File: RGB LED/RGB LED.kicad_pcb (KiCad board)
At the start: 2 copper layers, 93.1 x 66.5 mm, 86 parts, among them J1 USB_C_Receptacle_USB2.0_16P, SW1 SW_SPST_FSMSM, SW2 SW_SPST_FSMSM, U1 AP2112K-3.3, U2 MAX7219, U3 ESP32-S3-WROOM-1-N4

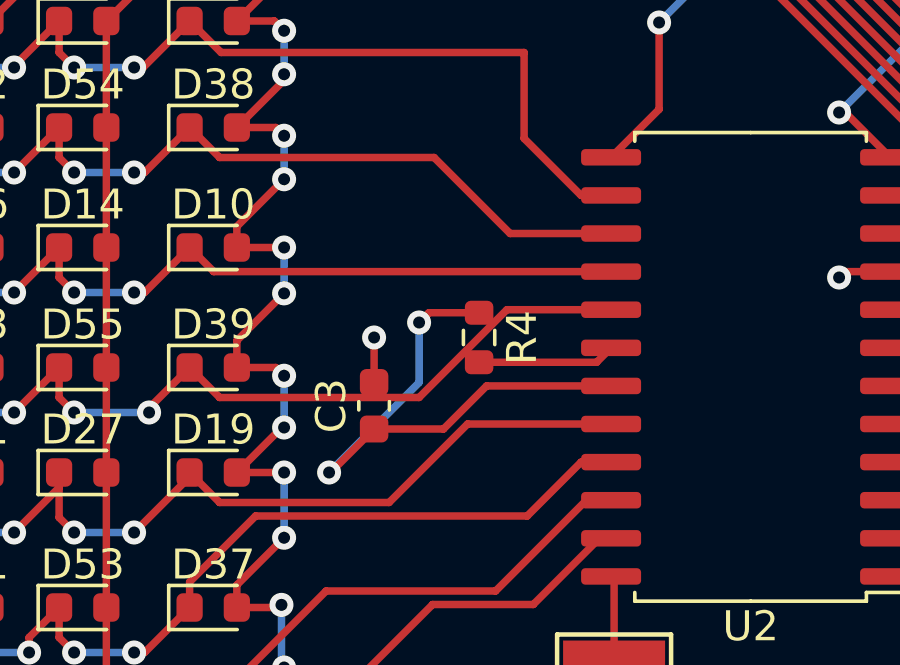
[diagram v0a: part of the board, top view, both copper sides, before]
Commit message: ran drc and edited according to drc
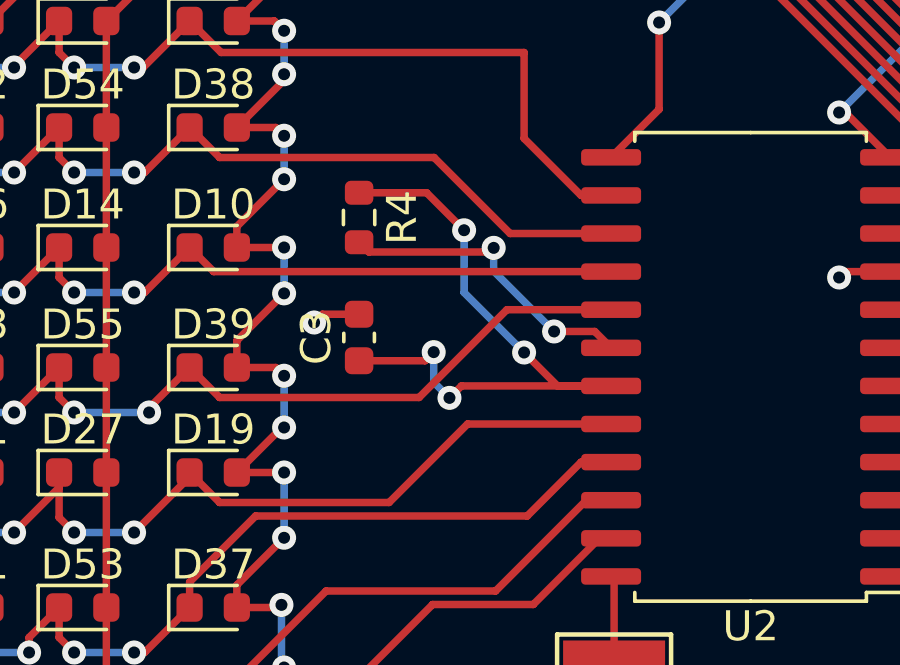
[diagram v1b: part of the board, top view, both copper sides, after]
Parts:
- moved R4 5.66 mm to (133.0, 81.5)
- moved C3 2.33 mm to (133.0, 85.5)
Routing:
- net Net-(U2-ISET): track 4.60 -> 10.4 mm, vias 0 -> 2
- net +5V: track 19.0 -> 22.2 mm, vias 2 -> 4
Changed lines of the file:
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@@
   )
   (footprint "Resistor_SMD:R_0603_1608Metric" (layer "F.Cu")
-    (at 137 85.5 -90)
+    (at 133 81.5 -90)
     (descr "Resistor SMD 0603 (1608 Metric), square (rectangular) end terminal, IPC_7351 nominal, (Body size source: IPC-SM-782 page 72, https://www.pcb-3d.com/wordpress/wp-content/uploads/ipc-sm-782a_amendment_1_and_2.pdf), generated with kicad-footprint-generator")
     (tags "resistor")
@@
   )
   (footprint "Capacitor_SMD:C_0603_1608Metric" (layer "F.Cu")
-    (at 133.5 87.775 90)
+    (at 133 85.5 90)
     (descr "Capacitor SMD 0603 (1608 Metric), square (rectangular) end terminal, IPC_7351 nominal, (Body size source: IPC-SM-782 page 76, https://www.pcb-3d.com/wordpress/wp-content/uploads/ipc-sm-782a_amendment_1_and_2.pdf), generated with kicad-footprint-generator")
     (tags "capacitor")
@@
   (segment (start 88 48.275) (end 88.775 48.275) (width 0.25) (layer "F.Cu") (net 2))
   (segment (start 78.775 46.225) (end 79 46) (width 0.25) (layer "F.Cu") (net 2))
-  (segment (start 133.5 87) (end 133.5 85.5) (width 0.25) (layer "F.Cu") (net 2))
   (segment (start 80.9374 48.8202) (end 79.6798 48.8202) (width 0.25) (layer "F.Cu") (net 2))
   (segment (start 111 65.8) (end 111 67.5) (width 0.25) (layer "F.Cu") (net 2))
   (segment (start 149.41 45) (end 147.5 45) (width 0.25) (layer "F.Cu") (net 2))
   (segment (start 156.275 61.275) (end 156.275 62.715) (width 0.25) (layer "F.Cu") (net 2))
+  (segment (start 131.775 84.725) (end 131.5 85) (width 0.25) (layer "F.Cu") (net 2))
   (segment (start 124.42 42.42) (end 124.5 42.5) (width 0.25) (layer "F.Cu") (net 2))
   (segment (start 117 46.225) (end 115.725 46.225) (width 0.25) (layer "F.Cu") (net 2))
   (segment (start 75.7 65.8) (end 75.4 65.5) (width 0.25) (layer "F.Cu") (net 2))
+  (segment (start 133 84.725) (end 131.775 84.725) (width 0.25) (layer "F.Cu") (net 2))
   (segment (start 88.775 48.275) (end 89.5 49) (width 0.25) (layer "F.Cu") (net 2))
   (segment (start 76.88 67.15) (end 76.88 68.38) (width 0.25) (layer "F.Cu") (net 2))
@@
   (segment (start 79.6798 48.8202) (end 79.5 49) (width 0.25) (layer "F.Cu") (net 2))
   (segment (start 83 67.825) (end 83 69.5) (width 0.25) (layer "F.Cu") (net 2))
-  (via (at 133.5 85.5) (size 0.8) (drill 0.4) (layers "F.Cu" "B.Cu") (net 2))
+  (via (at 131.5 85) (size 0.8) (drill 0.4) (layers "F.Cu" "B.Cu") (net 2))
   (via (at 156.265 62.725) (size 0.8) (drill 0.4) (layers "F.Cu" "B.Cu") (net 2))
   (via (at 115.5 46) (size 0.8) (drill 0.4) (layers "F.Cu" "B.Cu") (net 2))
@@
   (segment (start 138 49) (end 142.5 49) (width 0.25) (layer "B.Cu") (net 3))
   (segment (start 142.5 49) (end 150 56.5) (width 0.25) (layer "B.Cu") (net 3))
-  (segment (start 137 84.675) (end 135.325 84.675) (width 0.25) (layer "F.Cu") (net 4))
-  (segment (start 132 90) (end 132.05 90) (width 0.25) (layer "F.Cu") (net 4))
-  (segment (start 137.249604 87.114) (end 141.4002 87.114) (width 0.25) (layer "F.Cu") (net 4))
-  (segment (start 135.813604 88.55) (end 137.249604 87.114) (width 0.25) (layer "F.Cu") (net 4))
-  (segment (start 135.325 84.675) (end 135 85) (width 0.25) (layer "F.Cu") (net 4))
-  (segment (start 132.05 90) (end 133.5 88.55) (width 0.25) (layer "F.Cu") (net 4))
-  (segment (start 133.5 88.55) (end 135.813604 88.55) (width 0.25) (layer "F.Cu") (net 4))
-  (via (at 132 90) (size 0.8) (drill 0.4) (layers "F.Cu" "B.Cu") (net 4))
-  (via (at 135 85) (size 0.8) (drill 0.4) (layers "F.Cu" "B.Cu") (net 4))
-  (segment (start 135 87) (end 132 90) (width 0.25) (layer "B.Cu") (net 4))
-  (segment (start 135 85) (end 135 87) (width 0.25) (layer "B.Cu") (net 4))
+  (segment (start 136.411306 87.114) (end 141.4002 87.114) (width 0.25) (layer "F.Cu") (net 4))
+  (segment (start 136.5 81.925) (end 135.25 80.675) (width 0.25) (layer "F.Cu") (net 4))
+  (segment (start 133 86.275) (end 135.199694 86.275) (width 0.25) (layer "F.Cu") (net 4))
+  (segment (start 139.614 87.114) (end 141.4002 87.114) (width 0.25) (layer "F.Cu") (net 4))
+  (segment (start 135.199694 86.275) (end 135.487347 85.987347) (width 0.25) (layer "F.Cu") (net 4))
+  (segment (start 138.5 86) (end 139.614 87.114) (width 0.25) (layer "F.Cu") (net 4))
+  (segment (start 135.25 80.675) (end 133 80.675) (width 0.25) (layer "F.Cu") (net 4))
+  (segment (start 136.012653 87.512653) (end 136.411306 87.114) (width 0.25) (layer "F.Cu") (net 4))
+  (via (at 136.5 81.925) (size 0.8) (drill 0.4) (layers "F.Cu" "B.Cu") (net 4))
+  (via (at 135.487347 85.987347) (size 0.8) (drill 0.4) (layers "F.Cu" "B.Cu") (net 4))
+  (via (at 136.012653 87.512653) (size 0.8) (drill 0.4) (layers "F.Cu" "B.Cu") (net 4))
+  (via (at 138.5 86) (size 0.8) (drill 0.4) (layers "F.Cu" "B.Cu") (net 4))
+  (segment (start 135.487347 85.987347) (end 135.487347 86.987347) (width 0.25) (layer "B.Cu") (net 4))
+  (segment (start 135.487347 86.987347) (end 136.012653 87.512653) (width 0.25) (layer "B.Cu") (net 4))
+  (segment (start 136.5 84) (end 138.5 86) (width 0.25) (layer "B.Cu") (net 4))
+  (segment (start 136.5 81.925) (end 136.5 84) (width 0.25) (layer "B.Cu") (net 4))
   (segment (start 80.8422 47.775) (end 80.9374 47.8702) (width 0.25) (layer "F.Cu") (net 5))
   (segment (start 74.96505 61.963579) (end 74.96505 61.96505) (width 0.5) (layer "F.Cu") (net 5))
@@
   (segment (start 147 71) (end 143 75) (width 0.25) (layer "B.Cu") (net 28))
   (segment (start 147 60) (end 147 71) (width 0.25) (layer "B.Cu") (net 28))
-  (segment (start 137 86.325) (end 140.9192 86.325) (width 0.25) (layer "F.Cu") (net 58))
-  (segment (start 140.9192 86.325) (end 141.4002 85.844) (width 0.25) (layer "F.Cu") (net 58))
+  (segment (start 137.34844 82.65) (end 133.325 82.65) (width 0.25) (layer "F.Cu") (net 58))
+  (segment (start 140.8552 85.299) (end 141.4002 85.844) (width 0.25) (layer "F.Cu") (net 58))
+  (segment (start 137.486567 82.511873) (end 137.34844 82.65) (width 0.25) (layer "F.Cu") (net 58))
+  (segment (start 133.325 82.65) (end 133 82.325) (width 0.25) (layer "F.Cu") (net 58))
+  (segment (start 139.5 85.299) (end 140.8552 85.299) (width 0.25) (layer "F.Cu") (net 58))
+  (via (at 137.486567 82.511873) (size 0.8) (drill 0.4) (layers "F.Cu" "B.Cu") (net 58))
+  (via (at 139.5 85.299) (size 0.8) (drill 0.4) (layers "F.Cu" "B.Cu") (net 58))
+  (segment (start 137.486567 82.511873) (end 137.486567 83.285567) (width 0.25) (layer "B.Cu") (net 58))
+  (segment (start 137.486567 83.285567) (end 139.5 85.299) (width 0.25) (layer "B.Cu") (net 58))
   (segment (start 151.700199 80.764) (end 150.7002 80.764) (width 0.25) (layer "F.Cu") (net 59))
   (segment (start 128.925 74.95) (end 130.175 74.95) (width 0.25) (layer "F.Cu") (net 59))
